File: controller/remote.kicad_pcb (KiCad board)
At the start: 2 copper layers, 69 x 58.7 mm, 43 parts, among them J1 Conn_01x03, J2 Debug, J3 Conn_01x06, J4 Conn_01x08, J5 Conn_01x08, J6 Jumper, J7 MC130VX, Q1 MMBT3904, Q2 MMBT3904, SW1 SW_SPST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

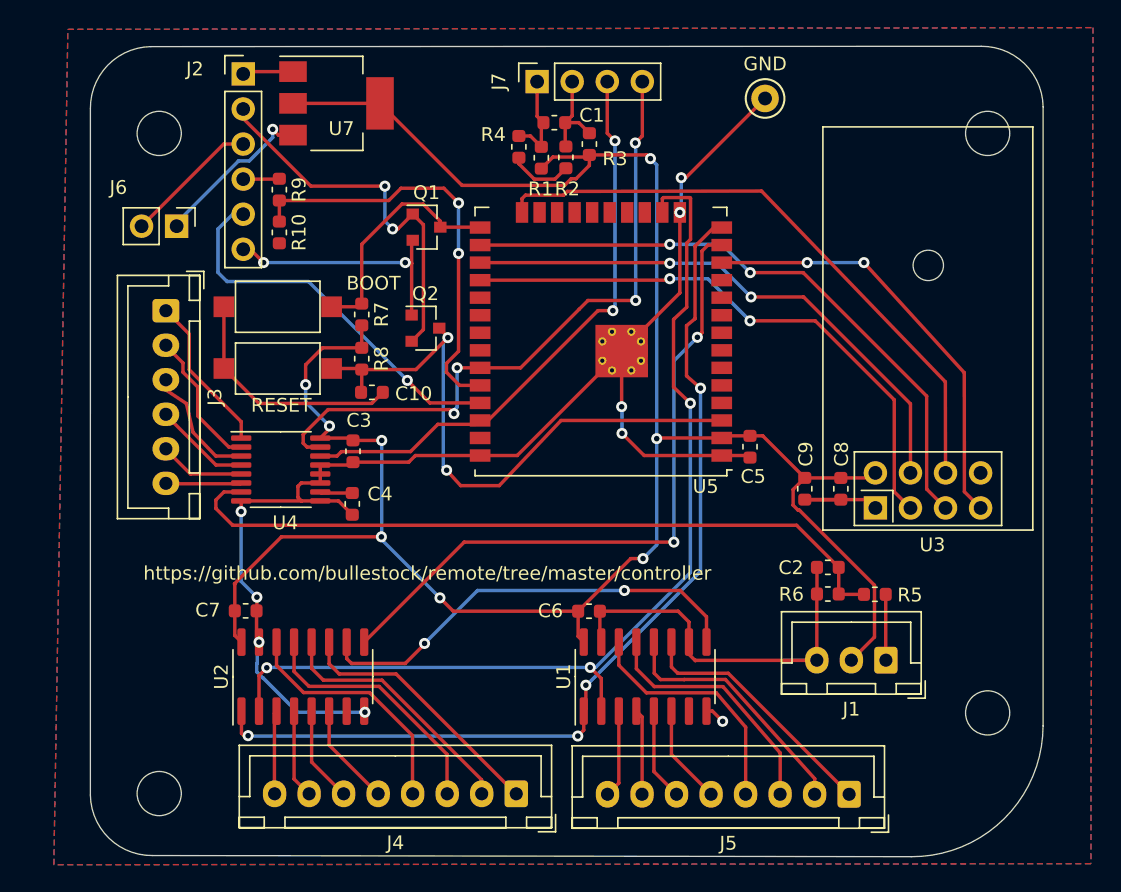
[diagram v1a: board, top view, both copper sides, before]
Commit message: Put ADC Vref onto analog connector.
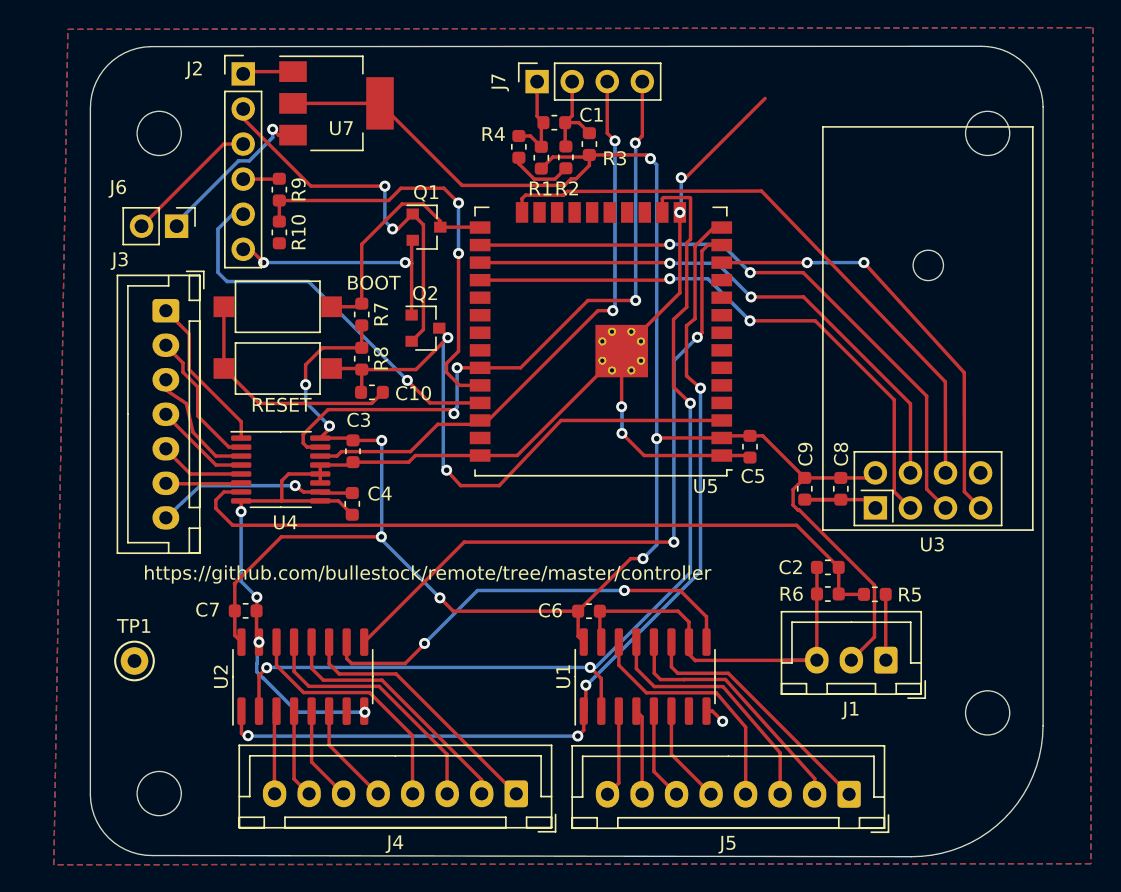
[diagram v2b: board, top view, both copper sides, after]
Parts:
- removed GND: TestPoint, TestPoint:TestPoint_Keystone_5000-5004_Miniature
- added TP1: TestPoint, TestPoint:TestPoint_Keystone_5000-5004_Miniature, F.Cu at (264.2, 137.2)
- J3: value Conn_01x06 -> Conn_01x07; footprint Connector_JST:JST_XH_B06B-XH-A_1x06_P2.50mm_Vertical -> Connector_JST:JST_XH_B07B-XH-A_1x07_P2.50mm_Vertical
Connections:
- C4 pad 1: Net-(U4-REF) -> Net-(J3-Pin_7)
- U4 pad 10: Net-(U4-REF) -> Net-(J3-Pin_7)
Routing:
- net Net-(J3-Pin_7): track 0.00 -> 14.6 mm, vias 0 -> 1
- net Net-(U4-REF): track 2.35 -> 0.00 mm
- net GND: track 163.9 -> 165.5 mm

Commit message: Remove nRF24L01.
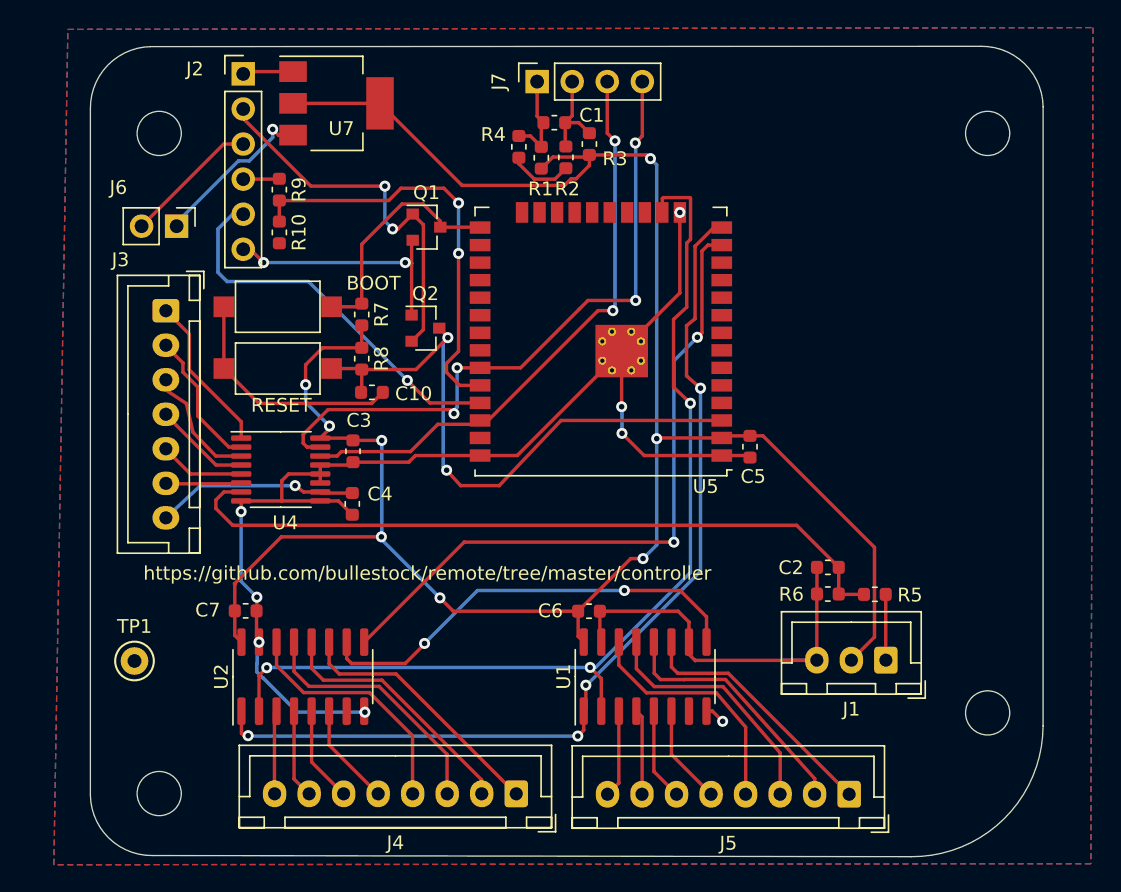
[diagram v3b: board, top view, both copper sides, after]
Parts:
- removed C8: 100n, Capacitor_SMD:C_0603_1608Metric
- removed C9: 10u, Capacitor_SMD:C_0603_1608Metric
- removed H5: MountingHole, MountingHole:MountingHole_2.2mm_M2
- removed U3: NRF24L01_Breakout, RF_Module:nRF24L01_Breakout
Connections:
- U5 pad 12: MISO -> unconnected-(U5-IO27-Pad12)
- U5 pad 24: MOSI -> unconnected-(U5-IO2-Pad24)
- U5 pad 26: SCK -> unconnected-(U5-IO4-Pad26)
- U5 pad 27: CS -> unconnected-(U5-IO16-Pad27)
- U5 pad 28: CE -> unconnected-(U5-IO17-Pad28)
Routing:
- net SCK: track 45.6 -> 0.00 mm, vias 2 -> 0
- net MOSI: track 44.3 -> 0.00 mm
- net CE: track 42.0 -> 0.00 mm, vias 2 -> 0
- net CS: track 40.4 -> 0.00 mm, vias 2 -> 0
- net MISO: track 31.4 -> 0.00 mm, vias 2 -> 0
- net GND: track 165.5 -> 146.6 mm, vias 9 -> 8
- net +3V3: track 163.3 -> 157.1 mm

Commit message: Power directly from battery.
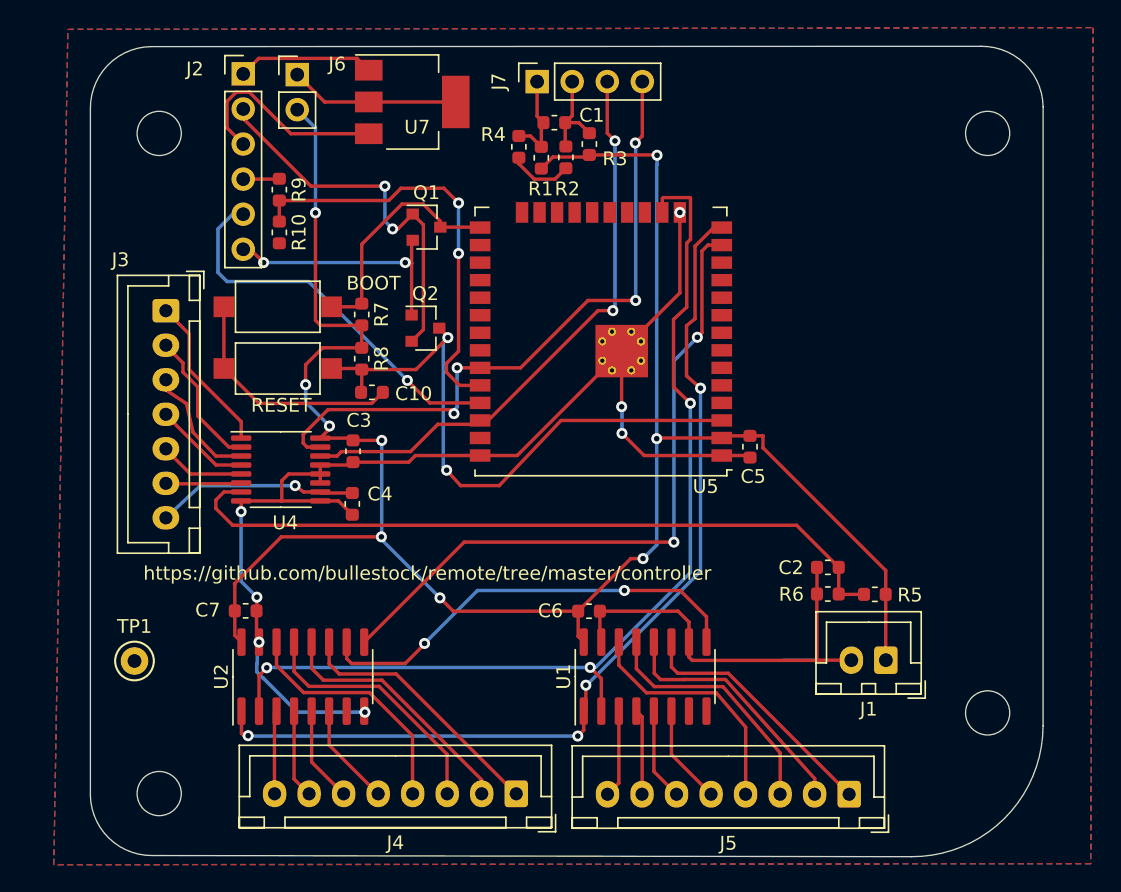
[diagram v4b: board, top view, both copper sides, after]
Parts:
- J1: value Conn_01x03 -> Conn_01x02; footprint Connector_JST:JST_XH_B03B-XH-A_1x03_P2.50mm_Vertical -> Connector_JST:JST_XH_B02B-XH-A_1x02_P2.50mm_Vertical
- moved J6 14.0 mm to (276.0, 94.7), turned to 0 degrees
- moved U7 5.49 mm to (284.3, 96.7)
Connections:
- C3 pad 1: +3V3 -> +BATT
- C5 pad 2: +3V3 -> +BATT
- C6 pad 1: +3V3 -> +BATT
- C7 pad 1: +3V3 -> +BATT
- J1 pad 2: +3V3 -> GND
- J2 pad 3: Net-(J2-Pin_3) -> +5V
- J6 pad 1: +5V -> Net-(J6-Pin_1)
- J6 pad 2: Net-(J2-Pin_3) -> +BATT
- R1 pad 2: +3V3 -> +BATT
- R3 pad 2: +3V3 -> +BATT
- R7 pad 2: +3V3 -> +BATT
- R8 pad 1: +3V3 -> +BATT
- U1 pad 16: +3V3 -> +BATT
- U2 pad 16: +3V3 -> +BATT
- U4 pad 16: +3V3 -> +BATT
- U5 pad 2: +3V3 -> +BATT
- U7 pad 2: +3V3 -> Net-(J6-Pin_1)
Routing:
- net +3V3: track 157.1 -> 0.00 mm, vias 8 -> 0
- net +BATT: track 4.77 -> 151.2 mm, vias 0 -> 9
- net Net-(J6-Pin_1): track 0.00 -> 12.3 mm
- net Net-(J2-Pin_3): track 9.82 -> 0.00 mm
- net GND: track 146.6 -> 154.0 mm, vias 8 -> 7
- net +5V: track 12.0 -> 15.4 mm, vias 1 -> 0

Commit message: Add large decoupling cap.
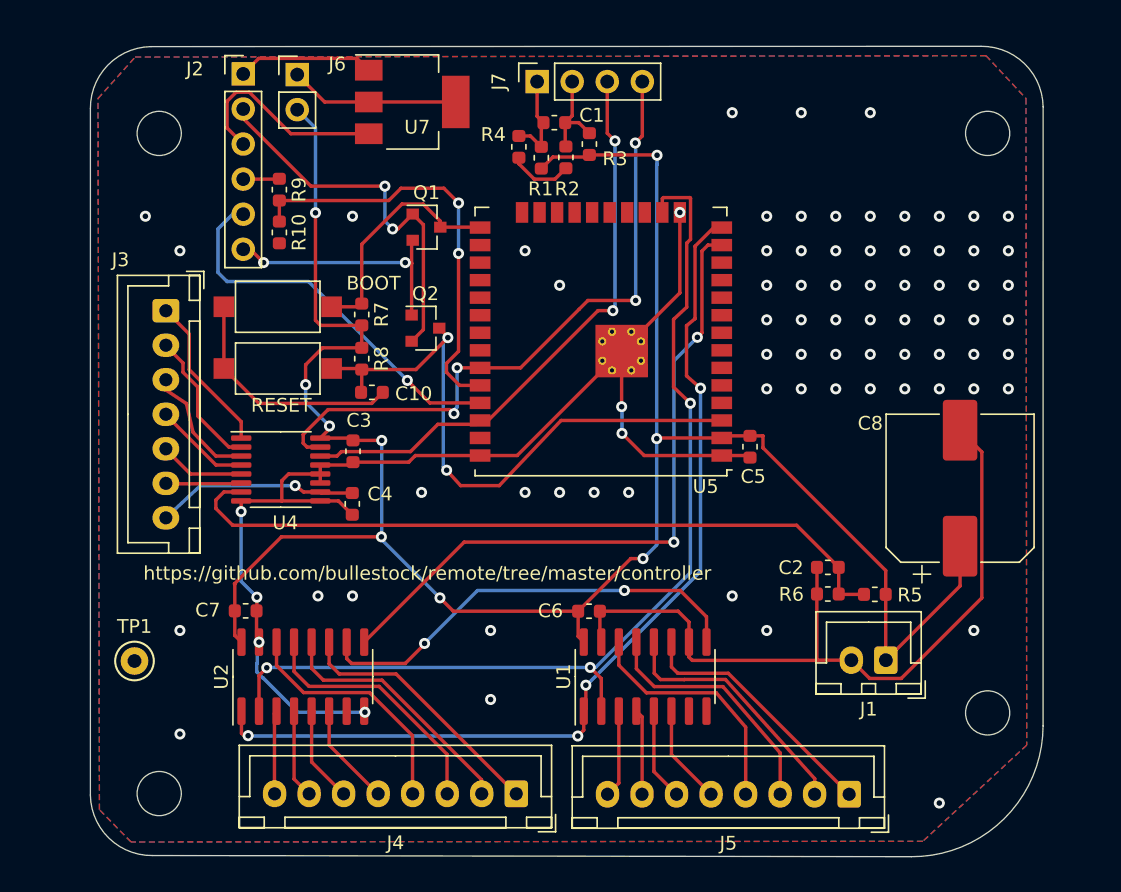
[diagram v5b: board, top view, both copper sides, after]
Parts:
- added C8: 220u/16V, Capacitor_SMD:CP_Elec_10x10.5, F.Cu at (324.0, 124.7)
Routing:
- net GND: track 154.0 -> 176.8 mm, vias 7 -> 78
- net +BATT: track 151.2 -> 161.7 mm

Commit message: Make mounting R1/R2 optional.
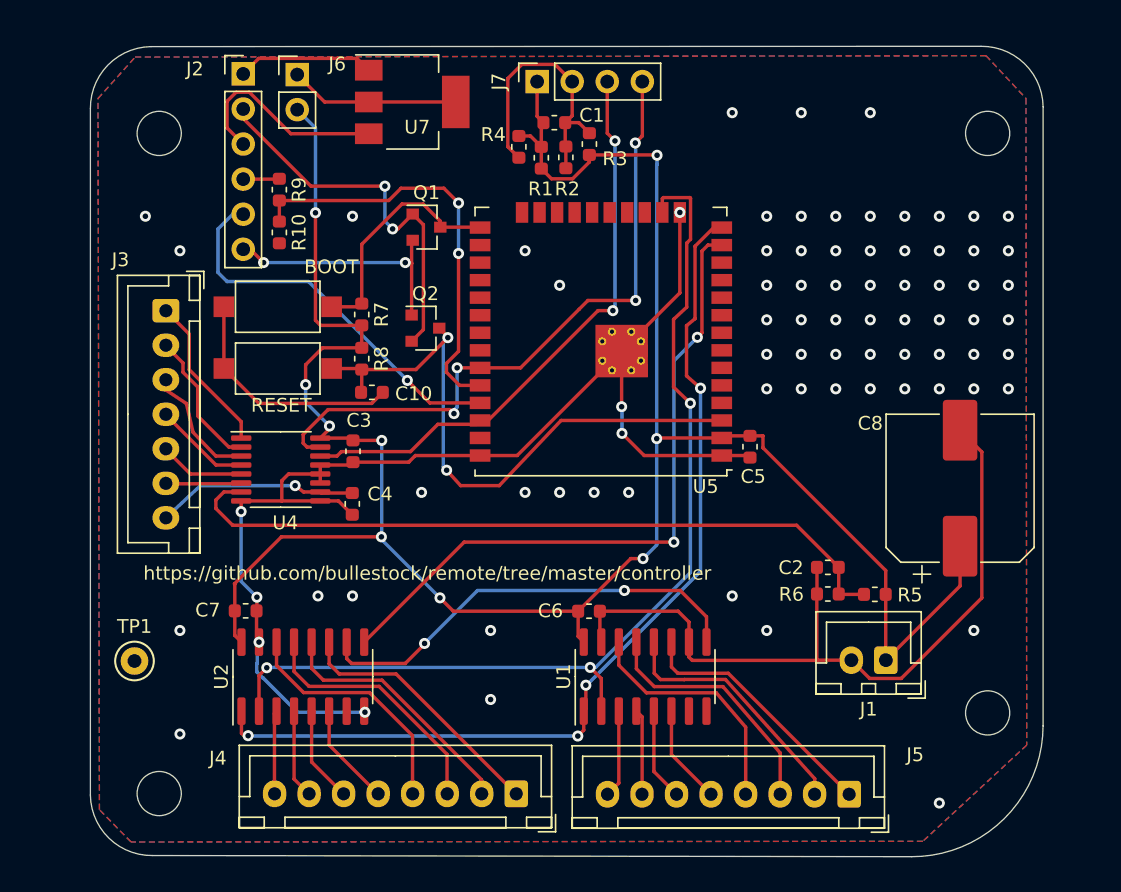
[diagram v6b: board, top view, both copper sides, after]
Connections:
- C1 pad 1: Net-(J7-Pin_2) -> GND
- C1 pad 2: Net-(J7-Pin_1) -> +BATT
- J7 pad 1: Net-(J7-Pin_1) -> +BATT
- J7 pad 2: Net-(J7-Pin_2) -> GND
- R1 pad 1: Net-(J7-Pin_1) -> +BATT
- R2 pad 1: Net-(J7-Pin_2) -> GND
- R3 pad 1: Net-(J7-Pin_2) -> GND
- R4 pad 1: Net-(J7-Pin_1) -> +BATT
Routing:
- net GND: track 176.8 -> 192.4 mm
- net +BATT: track 161.7 -> 171.3 mm
- net Net-(J7-Pin_2): track 6.99 -> 0.00 mm
- net Net-(J7-Pin_1): track 6.94 -> 0.00 mm

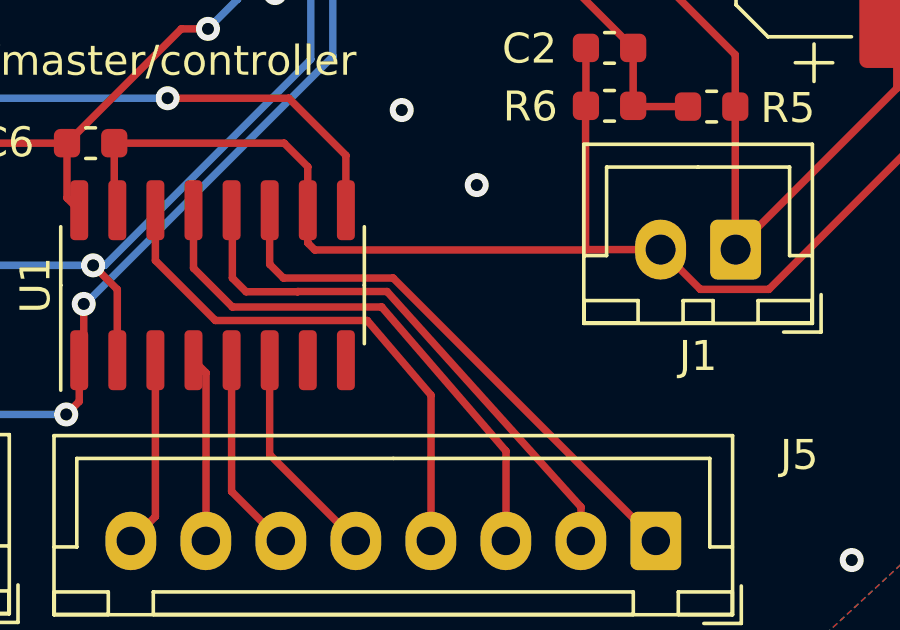
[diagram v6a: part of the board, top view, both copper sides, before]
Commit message: Fix missing trace.
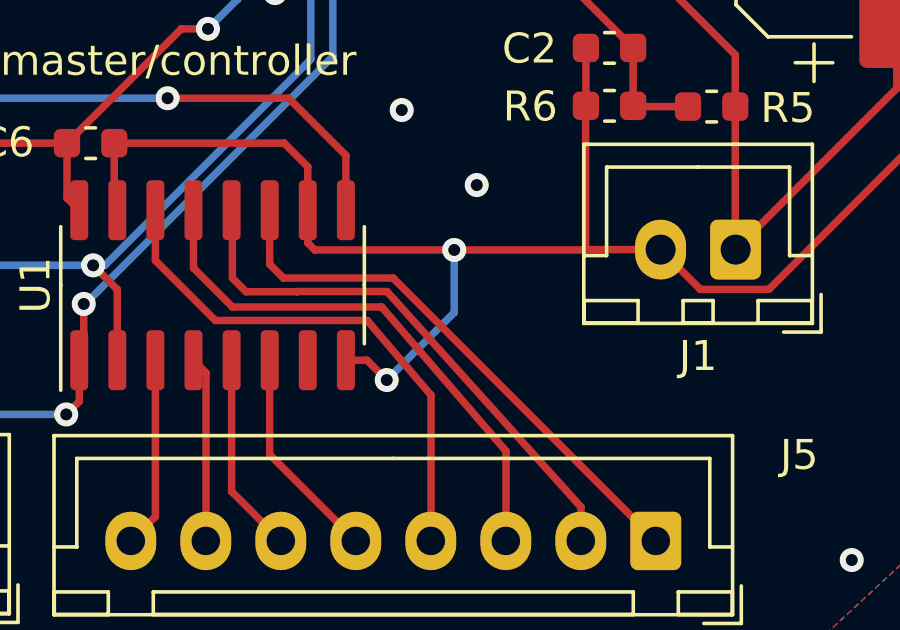
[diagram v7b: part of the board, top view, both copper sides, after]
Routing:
- net GND: track 192.4 -> 199.3 mm, vias 78 -> 80
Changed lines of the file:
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@@
-	)
-	(segment
-		(start 313.6163 137.1637)
-		(end 304.6005 137.1637)
-		(width 0.25)
-		(layer "F.Cu")
-		(net 1)
 	)
 	(segment
@@
 	)
 	(segment
+		(start 313.6163 137.1637)
+		(end 309.25 137.1637)
+		(width 0.25)
+		(layer "F.Cu")
+		(net 1)
+	)
+	(segment
 		(start 277.6651 123.6674)
 		(end 275.3666 123.6674)
@@
 	)
 	(segment
+		(start 306.3392 140.8392)
+		(end 307 141.5)
+		(width 0.25)
+		(layer "F.Cu")
+		(net 1)
+	)
+	(segment
 		(start 304.3682 134.3914)
 		(end 304.3682 135.8392)
@@
 	)
 	(segment
+		(start 309.25 137.1637)
+		(end 304.6005 137.1637)
+		(width 0.25)
+		(layer "F.Cu")
+		(net 1)
+	)
+	(segment
 		(start 295.4044 99.9005)
 		(end 295.4528 99.9489)
@@
 	)
 	(segment
+		(start 305.6382 140.8392)
+		(end 306.3392 140.8392)
+		(width 0.25)
+		(layer "F.Cu")
+		(net 1)
+	)
+	(segment
 		(start 280.8478 140.8684)
 		(end 280.8986 140.9192)
@@
 	)
 	(via
+		(at 309.25 137.1637)
+		(size 0.8)
+		(drill 0.4)
+		(layers "F.Cu" "B.Cu")
+		(net 1)
+	)
+	(via
 		(at 299.4914 118.7958)
 		(size 0.8)
@@
 		(layers "F.Cu" "B.Cu")
 		(free yes)
+		(net 1)
+	)
+	(via
+		(at 307 141.5)
+		(size 0.8)
+		(drill 0.4)
+		(layers "F.Cu" "B.Cu")
 		(net 1)
 	)
@@
 		(width 0.25)
 		(layer "B.Cu")
+		(net 1)
+	)
+	(segment
+		(start 307 141.5)
+		(end 309.25 139.25)
+		(width 0.25)
+		(layer "B.Cu")
+		(net 1)
+	)
+	(segment
+		(start 309.25 139.25)
+		(end 309.25 137.1637)
+		(width 0.25)
+		(layer "B.Cu")
